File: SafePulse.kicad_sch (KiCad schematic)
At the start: 87 parts, among them IC1 S-35770E01I-K8T2U, J1 Conn_01x03_Male, J2 4208, Q1 FQT7N10L, Q2 BC846A, Q3 MMBT3906, Q4 MMBT3906, U1 TS4061AICT-1.25, U2 74HC14, U3 TLV27L1DBVT, U33 MAX9910EXK+T, U4 CD14538BM

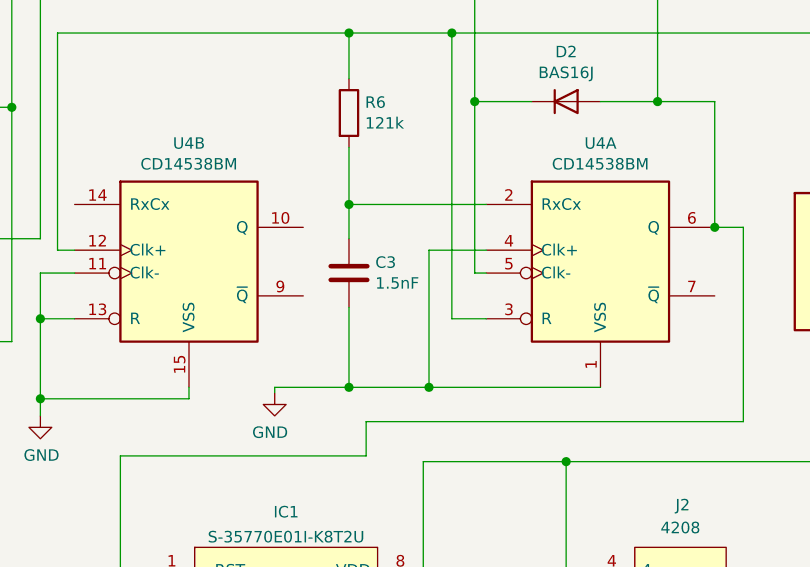
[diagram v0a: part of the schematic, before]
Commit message: Change C3 from 1.5nF to 1nF
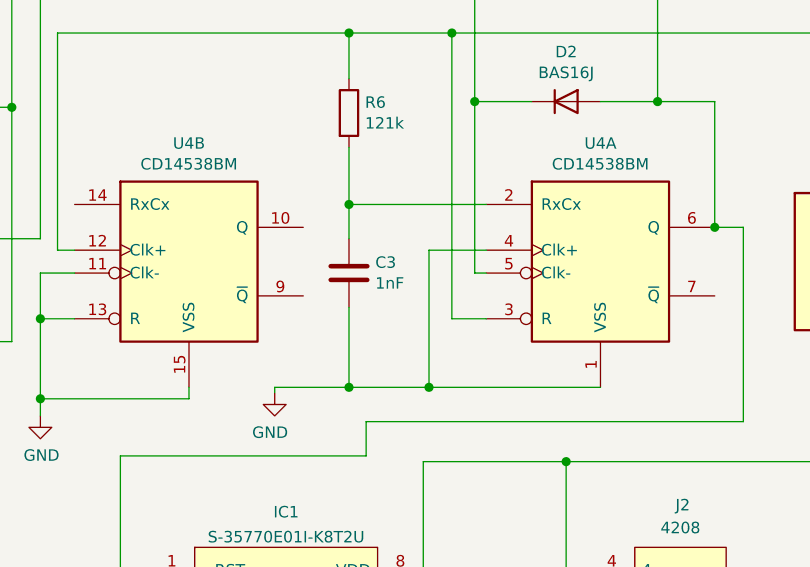
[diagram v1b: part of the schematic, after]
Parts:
- C3: value 1.5nF -> 1nF
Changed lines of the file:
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@@
 			)
 		)
-		(property "Value" "1.5nF"
+		(property "Value" "1nF"
 			(at 104.521 150.368 0)
 			(effects
